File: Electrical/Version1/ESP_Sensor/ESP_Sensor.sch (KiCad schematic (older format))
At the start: 44 parts, among them J1 Power 5V-24V, J2 Programming serial IO, J3 Conn_01x08_Female, Q1 BC817, Q2 BC817, Q3 BC817, Q4 BC817, SW1 Reset, SW2 Prog, U1 TLP291-4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

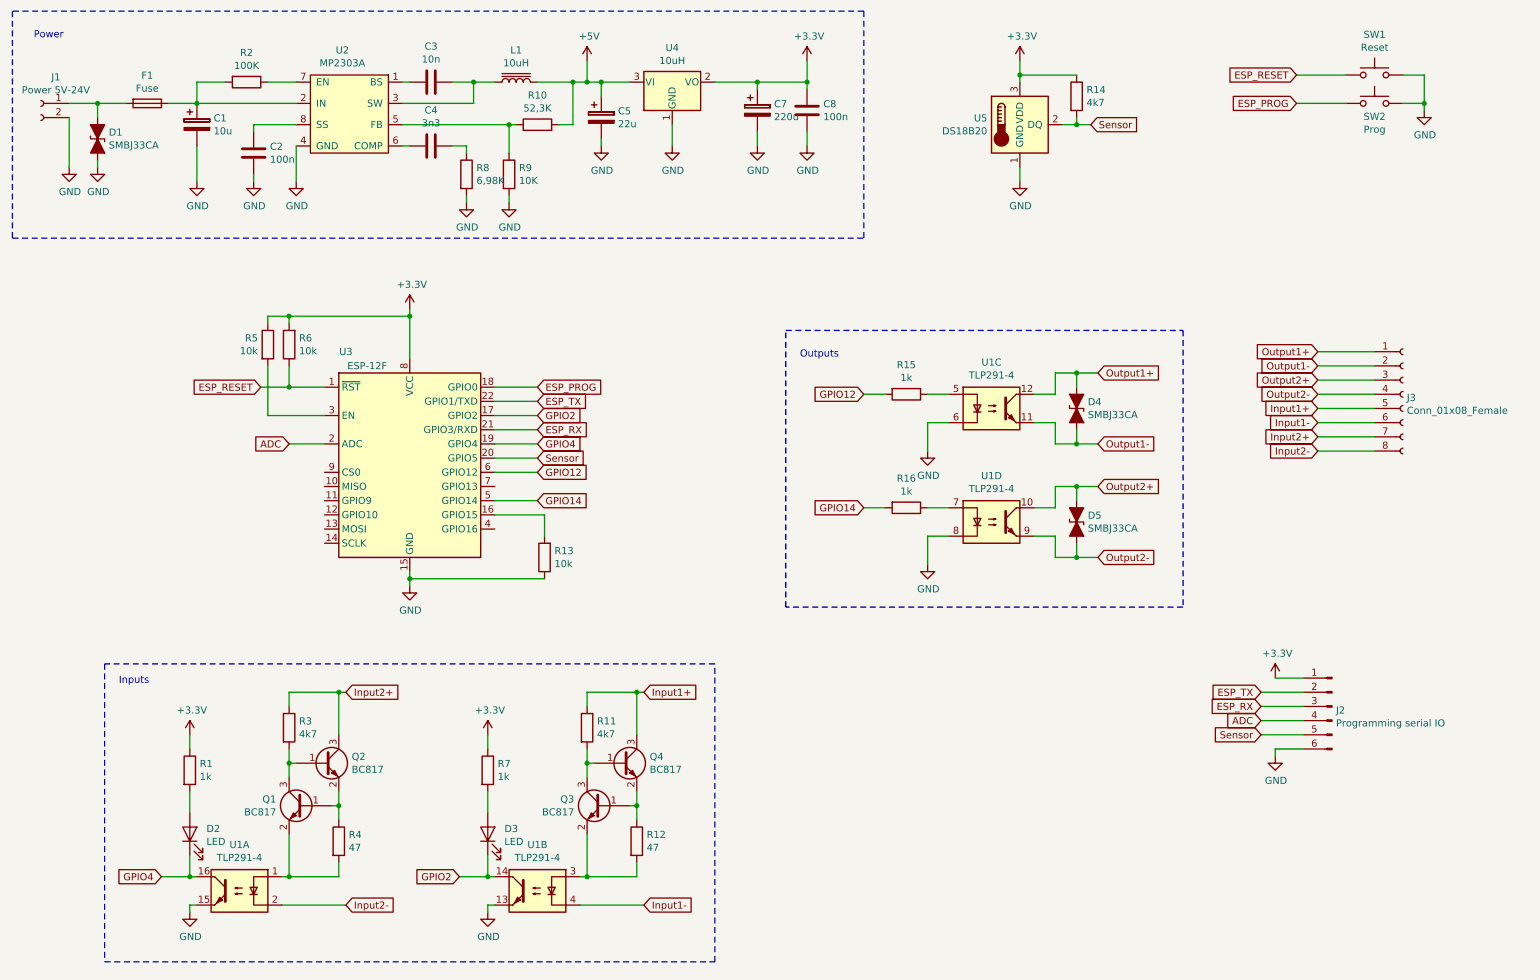
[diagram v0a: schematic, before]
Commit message: Updated pcb board with smd caps
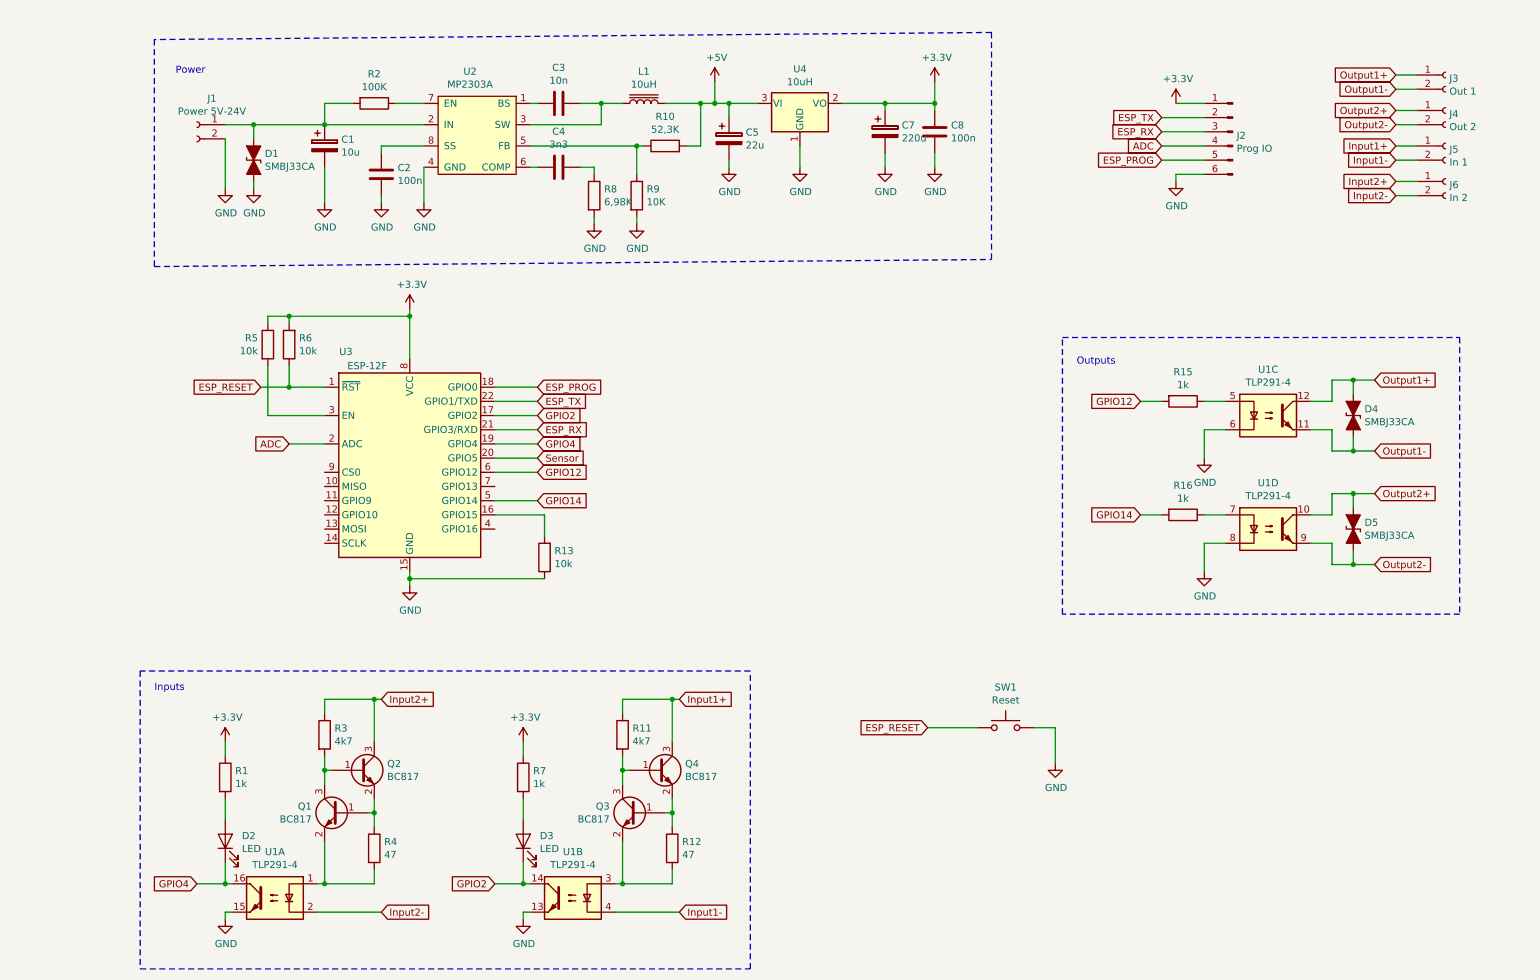
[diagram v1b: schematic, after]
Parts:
- removed F1: Fuse, Fuse:Fuse_Littelfuse-LVR100, symbol Device:Fuse
- removed J3: Conn_01x08_Female, TerminalBlock_Phoenix:TerminalBlock_Phoenix_MKDS-1,5-8_1x08_P5.00mm_Horizontal, symbol Connector:Conn_01x08_Female
- removed R14: 4k7, Resistor_SMD:R_0805_2012Metric_Pad1.15x1.40mm_HandSolder, symbol Device:R
- removed SW2: Prog, Button_Switch_THT:SW_PUSH_6mm_H7.3mm, symbol Switch:SW_Push
- removed U5: DS18B20, Package_TO_SOT_THT:TO-92_Inline, symbol Sensor_Temperature:DS18B20
- added J3: Out 1, TerminalBlock_Phoenix:TerminalBlock_Phoenix_MKDS-1,5-2_1x02_P5.00mm_Horizontal, symbol Connector:Conn_01x02_Female
- added J4: Out 2, TerminalBlock_Phoenix:TerminalBlock_Phoenix_MKDS-1,5-2_1x02_P5.00mm_Horizontal, symbol Connector:Conn_01x02_Female
- added J5: In 1, TerminalBlock_Phoenix:TerminalBlock_Phoenix_MKDS-1,5-2_1x02_P5.00mm_Horizontal, symbol Connector:Conn_01x02_Female
- added J6: In 2, TerminalBlock_Phoenix:TerminalBlock_Phoenix_MKDS-1,5-2_1x02_P5.00mm_Horizontal, symbol Connector:Conn_01x02_Female
- C2, C3, C4, C8: footprint Capacitor_THT:C_Rect_L7.2mm_W2.5mm_P5.00mm_FKS2_FKP2_MKS2_MKP2 -> Capacitor_SMD:C_0805_2012Metric_Pad1.15x1.40mm_HandSolder
- J2: value Programming serial IO -> Prog IO
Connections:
- net ESP_PROG: now also J2.5 (Pin_5)
- net Input1+: now also J5.1 (Pin_1)
- net Input1-: now also J5.2 (Pin_2)
- net Input2+: now also J6.1 (Pin_1)
- net Input2-: now also J6.2 (Pin_2)
- net Output1+: now also J3.1 (Pin_1)
- net Output1-: now also J3.2 (Pin_2)
- net Output2+: now also J4.1 (Pin_1)
- net Output2-: now also J4.2 (Pin_2)
- net Sensor: no longer J2.5 (Pin_5)
- net at D1.1 (A1), J1.1 (Pin_1): now also C1.1, R2.2, U2.2 (IN)
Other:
- moved on the sheet: C1, C2, C3, C4, C5, C7, C8, D1, D2, D3, D4, D5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
